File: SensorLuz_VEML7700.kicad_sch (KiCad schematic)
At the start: 0 parts

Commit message: Protocolos I2C/SPI
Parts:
- added LED1: VEML7700-TR, easyeda2kicad:LED-SMD_4P-L6.8-W2.4_VEML7700-TR, symbol CANSAT_STM32_symbols:VEML7700-TR
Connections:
- new net I2C1_SCL: LED1.1 (SCL)
- new net I2C1_SDA: LED1.4 (SDA)
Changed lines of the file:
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@@
 	(generator_version "10.0")
 	(paper "A4")
+	(global_label "I2C1_SDA"
+		(shape input)
+		(at 123.19 86.36 180)
+		(fields_autoplaced yes)
+		(effects
+			(font
+				(size 1.27 1.27)
+			)
+			(justify right)
+		)
+		(property "Intersheetrefs" "${INTERSHEET_REFS}"
+			(at 111.3753 86.36 0)
+			(hide yes)
+			(show_name no)
+			(do_not_autoplace no)
+			(effects
+				(font
+					(size 1.27 1.27)
+				)
+				(justify right)
+			)
+		)
+	)
+	(global_label "I2C1_SCL"
+		(shape input)
+		(at 123.19 78.74 180)
+		(fields_autoplaced yes)
+		(effects
+			(font
+				(size 1.27 1.27)
+			)
+			(justify right)
+		)
+		(property "Intersheetrefs" "${INTERSHEET_REFS}"
+			(at 111.4358 78.74 0)
+			(hide yes)
+			(show_name no)
+			(do_not_autoplace no)
+			(effects
+				(font
+					(size 1.27 1.27)
+				)
+				(justify right)
+			)
+		)
+	)
+	(symbol
+		(lib_id "CANSAT_STM32_symbols:VEML7700-TR")
+		(at 128.27 82.55 0)
+		(unit 1)
+		(body_style 1)
+		(exclude_from_sim no)
+		(in_bom yes)
+		(on_board yes)
+		(in_pos_files yes)
+		(dnp no)
+		(fields_autoplaced yes)
+		(property "Reference" "LED1"
+			(at 134.62 81.2799 0)
+			(show_name no)
+			(do_not_autoplace no)
+			(effects
+				(font
+					(size 1.27 1.27)
+				)
+				(justify left)
+			)
+		)
+		(property "Value" "VEML7700-TR"
+			(at 134.62 83.8199 0)
+			(show_name no)
+			(do_not_autoplace no)
+			(effects
+				(font
+					(size 1.27 1.27)
+				)
+				(justify left)
+			)
+		)
+		(property "Footprint" "easyeda2kicad:LED-SMD_4P-L6.8-W2.4_VEML7700-TR"
+			(at 128.27 93.98 0)
+			(hide yes)
+			(show_name no)
+			(do_not_autoplace no)
+			(effects
+				(font
+					(size 1.27 1.27)
+				)
+			)
+		)
+		(property "Datasheet" "https://www.lcsc.com/datasheet/C504893.pdf"
+			(at 128.27 96.52 0)
+			(hide yes)
+			(show_name no)
+			(do_not_autoplace no)
+			(effects
+				(font
+					(size 1.27 1.27)
+				)
+			)
+		)
+		(property "Description" ""
+			(at 128.27 82.55 0)
+			(hide yes)
+			(show_name no)
+			(do_not_autoplace no)
+			(effects
+				(font
+					(size 1.27 1.27)
+				)
+			)
+		)
+		(property "Manufacturer" "VISHAY(威世)"
+			(at 128.27 99.06 0)
+			(hide yes)
+			(show_name no)
+			(do_not_autoplace no)
+			(effects
+				(font
+					(size 1.27 1.27)
+				)
+			)
+		)
+		(property "MPN" "VEML7700-TR"
+			(at 128.27 101.6 0)
+			(hide yes)
+			(show_name no)
+			(do_not_autoplace no)
+			(effects
+				(font
+					(size 1.27 1.27)
+				)
+			)
+		)
+		(property "LCSC Part" "C504893"
+			(at 128.27 104.14 0)
+			(hide yes)
+			(show_name no)
+			(do_not_autoplace no)
+			(effects
+				(font
+					(size 1.27 1.27)
+				)
+			)
+		)
+		(pin "3"
+		)
+		(pin "2"
+		)
+		(pin "1"
+		)
+		(pin "4"
+		)
+		(instances
+			(project "ARLISS_STM32_2026"
+				(path "/9719ea46-14c4-4409-9c57-49dd5454c03f/90e9a371-b783-4b2a-a8c2-544713e1ebd2"
+					(reference "LED1")
+					(unit 1)
+				)
+			)
+		)
+	)
 )

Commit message: Todo menos alimentación
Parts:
- added C31: 100nF, easyeda2kicad:C0402, symbol CANSAT_STM32_symbols:TCC0402X7R104J500AT
- added C32: 10uF, easyeda2kicad:CAP-SMD_BD6.3-L6.6-W6.6-LS7.3, symbol CANSAT_STM32_symbols:UUA1H100MCL1GS
- added JP1: SolderJumper_2_Open, symbol Jumper:SolderJumper_2_Open
- added R9: 10, symbol Device:R
- added U10: Green LED, easyeda2kicad:LED0603-FD, symbol CANSAT_STM32_symbols:YLED0603G
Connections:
- net VDD_LUZ: now reaches LED1.2 (VDD)
- net VDD_LUZ: now also C31.2, C32.1, R9.2, U10.1 (+)
- net GND: now reaches LED1.3 (GND)
- net GND: now also C31.1, C32.2, JP1.1 (A)
- net I2C1_SCL renamed I2C2_SCL
- net I2C1_SDA renamed I2C2_SDA
- new net: JP1.2 (B), U10.2 (-)
- new net +3V3: R9.1

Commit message: ALIMENTACIÓN
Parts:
- R9: footprint (none) -> Resistor_SMD:R_0402_1005Metric_Pad0.72x0.64mm_HandSolder; LCSC (none) -> C854481
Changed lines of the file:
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@@
 			)
 		)
-		(property "Footprint" ""
+		(property "Footprint" "Resistor_SMD:R_0402_1005Metric_Pad0.72x0.64mm_HandSolder"
 			(at 60.96 83.058 90)
 			(hide yes)
@@
 			(hide yes)
 			(show_name no)
+			(do_not_autoplace no)
+			(effects
+				(font
+					(size 1.27 1.27)
+				)
+			)
+		)
+		(property "LCSC" "C854481"
+			(at 60.96 81.28 90)
+			(hide yes)
+			(show_name no)

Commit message: Cantidad de errores en la PCB: 29
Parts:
- C31: footprint easyeda2kicad:C0402 -> ARLISS-footprints:C0402
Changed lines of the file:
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@@
 			)
 		)
-		(property "Footprint" "easyeda2kicad:C0402"
+		(property "Footprint" "ARLISS-footprints:C0402"
 			(at 82.55 91.44 0)
 			(hide yes)

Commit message: Cantidad de errores de la placa: 05
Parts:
- C32: footprint easyeda2kicad:CAP-SMD_BD6.3-L6.6-W6.6-LS7.3 -> ARLISS-footprints:CAP-SMD_BD6.3-L6.6-W6.6-LS7.3
- LED1: footprint easyeda2kicad:LED-SMD_4P-L6.8-W2.4_VEML7700-TR -> ARLISS-footprints:LED-SMD_4P-L6.8-W2.4_VEML7700-TR
- U10: footprint easyeda2kicad:LED0603-FD -> ARLISS-footprints:LED0603-FD
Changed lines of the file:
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@@
 			)
 		)
-		(property "Footprint" "easyeda2kicad:LED-SMD_4P-L6.8-W2.4_VEML7700-TR"
+		(property "Footprint" "ARLISS-footprints:LED-SMD_4P-L6.8-W2.4_VEML7700-TR"
 			(at 128.27 93.98 0)
 			(hide yes)
@@
 			)
 		)
-		(property "Footprint" "easyeda2kicad:CAP-SMD_BD6.3-L6.6-W6.6-LS7.3"
+		(property "Footprint" "ARLISS-footprints:CAP-SMD_BD6.3-L6.6-W6.6-LS7.3"
 			(at 83.82 91.44 0)
 			(hide yes)
@@
 			)
 		)
-		(property "Footprint" "easyeda2kicad:LED0603-FD"
+		(property "Footprint" "ARLISS-footprints:LED0603-FD"
 			(at 160.02 83.82 0)
 			(hide yes)

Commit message: Cantidad de errores en la placa: 04
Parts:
- JP1: footprint (none) -> Jumper:SolderJumper-2_P1.3mm_Open_TrianglePad1.0x1.5mm
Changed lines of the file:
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@@
 			)
 		)
-		(property "Footprint" ""
+		(property "Footprint" "Jumper:SolderJumper-2_P1.3mm_Open_TrianglePad1.0x1.5mm"
 			(at 167.64 96.52 0)
 			(hide yes)

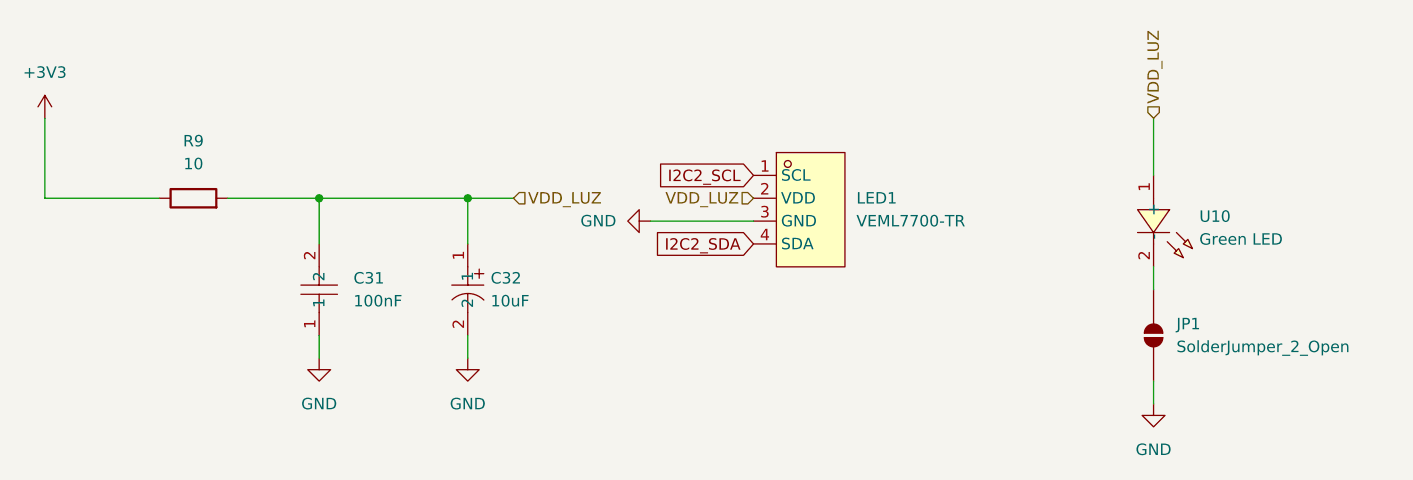
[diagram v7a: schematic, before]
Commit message: Esquemático Versión mejorada
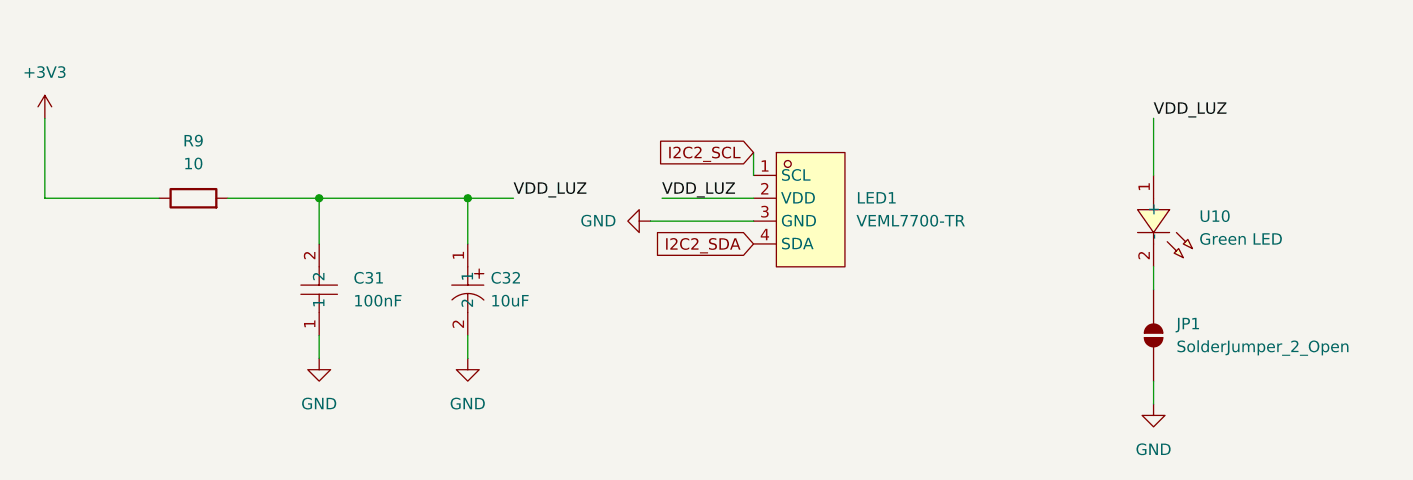
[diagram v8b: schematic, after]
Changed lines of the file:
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@@
+	(wire
+		(pts
+			(xy 123.19 76.2) (xy 123.19 78.74)
+		)
+		(stroke
+			(width 0)
+			(type default)
+		)
+	)
 	(wire
 		(pts
@@
 		(pts
 			(xy 74.93 81.28) (xy 91.44 81.28)
+		)
+		(stroke
+			(width 0)
+			(type default)
+		)
+	)
+	(wire
+		(pts
+			(xy 113.03 81.28) (xy 123.19 81.28)
 		)
 		(stroke
@@
 		)
 	)
+	(label "VDD_LUZ"
+		(at 96.52 81.28 0)
+		(effects
+			(font
+				(size 1.27 1.27)
+			)
+			(justify left bottom)
+		)
+	)
+	(label "VDD_LUZ"
+		(at 167.64 72.39 0)
+		(effects
+			(font
+				(size 1.27 1.27)
+			)
+			(justify left bottom)
+		)
+	)
+	(label "VDD_LUZ"
+		(at 113.03 81.28 0)
+		(effects
+			(font
+				(size 1.27 1.27)
+			)
+			(justify left bottom)
+		)
+	)
 	(global_label "I2C2_SDA"
 		(shape input)
@@
 	(global_label "I2C2_SCL"
 		(shape input)
-		(at 123.19 78.74 180)
+		(at 123.19 76.2 180)
 		(fields_autoplaced yes)
 		(effects
@@
 		)
 		(property "Intersheetrefs" "${INTERSHEET_REFS}"
-			(at 111.4358 78.74 0)
+			(at 111.4358 76.2 0)
 			(hide yes)
 			(show_name no)
@@
 		)
 	)
-	(hierarchical_label "VDD_LUZ"
-		(shape input)
-		(at 167.64 72.39 90)
-		(effects
-			(font
-				(size 1.27 1.27)
-			)
-			(justify left)
-		)
-	)
-	(hierarchical_label "VDD_LUZ"
-		(shape input)
-		(at 123.19 81.28 180)
-		(effects
-			(font
-				(size 1.27 1.27)
-			)
-			(justify right)
-		)
-	)
-	(hierarchical_label "VDD_LUZ"
-		(shape input)
-		(at 96.52 81.28 0)
-		(effects
-			(font
-				(size 1.27 1.27)
-			)
-			(justify left)
-		)
-	)
